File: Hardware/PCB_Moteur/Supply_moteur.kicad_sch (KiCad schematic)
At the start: 27 parts, among them J1 XT30PW-F, U1 L6981N33DR

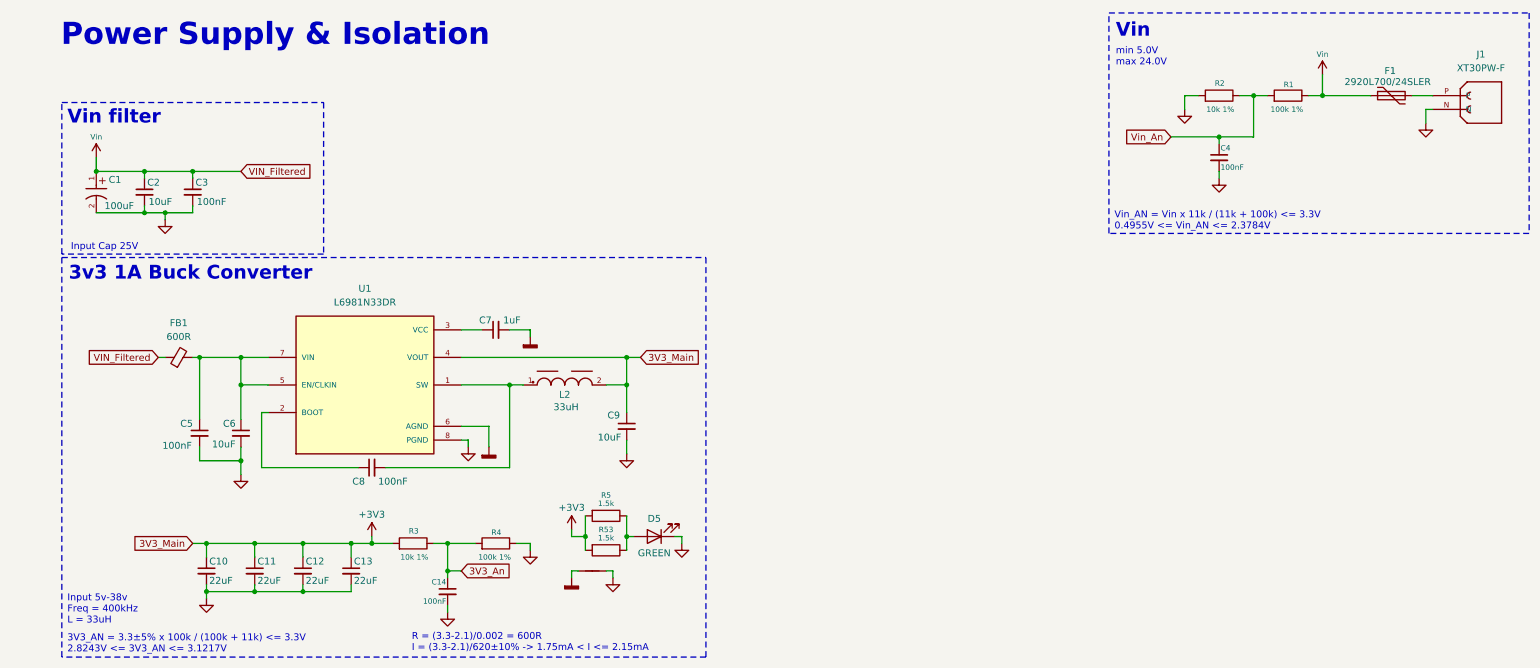
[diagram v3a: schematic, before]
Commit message: wip : reorder refdes and fix footprints
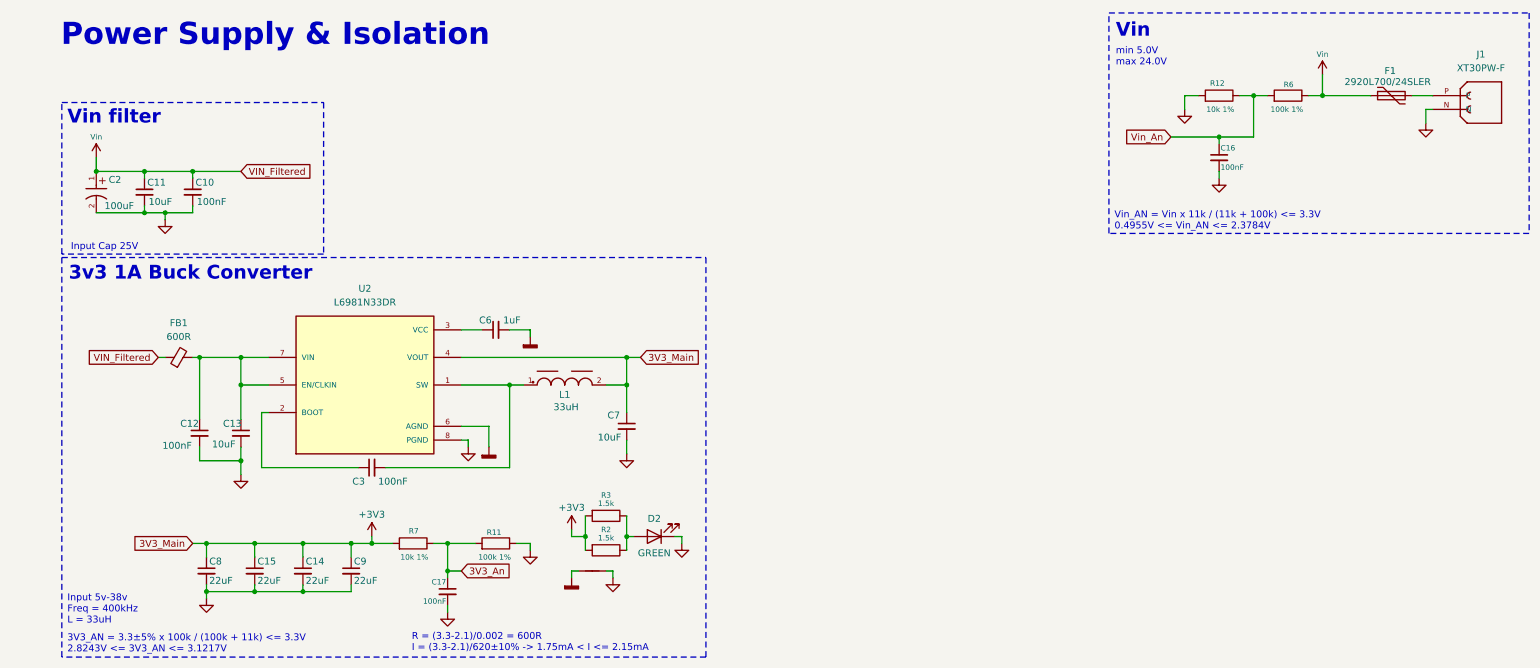
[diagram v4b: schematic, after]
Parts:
- renumbered C3 to C10, C2 to C11, C5 to C12, C6 to C13, C12 to C14, C11 to C15, C4 to C16, C14 to C17, C1 to C2, C8 to C3, C7 to C6, C9 to C7, C10 to C8, C13 to C9, D5 to D2, L2 to L1, NT4 to NT0, R4 to R11, R2 to R12, R53 to R2, R5 to R3, R1 to R6, R3 to R7, U1 to U2
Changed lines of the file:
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@@
 		(on_board yes)
 		(dnp no)
-		(property "Reference" "R4"
+		(property "Reference" "R11"
 			(at 94.996 108.458 90)
 			(effects
@@
 			(project "PCB_moteur"
 				(path "/b0d87684-7b1c-41d8-8358-755aa327573e/92d1df5d-a307-4eea-a65c-ade4cb0ad548"
-					(reference "R4")
+					(reference "R11")
 					(unit 1)
 				)
@@
 		(dnp no)
 		(fields_autoplaced yes)
-		(property "Reference" "NT4"
+		(property "Reference" "NT0"
 			(at 111.76 110.49 0)
 			(effects
@@
 			(project "PCB_moteur"
 				(path "/b0d87684-7b1c-41d8-8358-755aa327573e/92d1df5d-a307-4eea-a65c-ade4cb0ad548"
-					(reference "NT4")
+					(reference "NT0")
 					(unit 1)
 				)
@@
 		(on_board yes)
 		(dnp no)
-		(property "Reference" "C11"
+		(property "Reference" "C15"
 			(at 50.038 113.792 0)
 			(effects
@@
 			(project "PCB_moteur"
 				(path "/b0d87684-7b1c-41d8-8358-755aa327573e/92d1df5d-a307-4eea-a65c-ade4cb0ad548"
-					(reference "C11")
+					(reference "C15")
 					(unit 1)
 				)
@@
 		(on_board yes)
 		(dnp no)
-		(property "Reference" "R3"
+		(property "Reference" "R7"
 			(at 79.756 108.204 90)
 			(effects
@@
 			(project "PCB_moteur"
 				(path "/b0d87684-7b1c-41d8-8358-755aa327573e/92d1df5d-a307-4eea-a65c-ade4cb0ad548"
-					(reference "R3")
+					(reference "R7")
 					(unit 1)
 				)
@@
 		(on_board yes)
 		(dnp no)
-		(property "Reference" "R2"
+		(property "Reference" "R12"
 			(at 228.346 25.654 90)
 			(effects
@@
 			(project "PCB_moteur"
 				(path "/b0d87684-7b1c-41d8-8358-755aa327573e/92d1df5d-a307-4eea-a65c-ade4cb0ad548"
-					(reference "R2")
+					(reference "R12")
 					(unit 1)
 				)
@@
 		(on_board yes)
 		(dnp no)
-		(property "Reference" "D5"
+		(property "Reference" "D2"
 			(at 123.19 105.918 0)
 			(effects
@@
 			(project "PCB_moteur"
 				(path "/b0d87684-7b1c-41d8-8358-755aa327573e/92d1df5d-a307-4eea-a65c-ade4cb0ad548"
-					(reference "D5")
+					(reference "D2")
 					(unit 1)
 				)
@@
 		(on_board yes)
 		(dnp no)
-		(property "Reference" "C6"
+		(property "Reference" "C13"
 			(at 43.688 88.392 0)
 			(effects
@@
 			(project "PCB_moteur"
 				(path "/b0d87684-7b1c-41d8-8358-755aa327573e/92d1df5d-a307-4eea-a65c-ade4cb0ad548"
-					(reference "C6")
+					(reference "C13")
 					(unit 1)
 				)
@@
 		(on_board yes)
 		(dnp no)
-		(property "Reference" "C7"
+		(property "Reference" "C6"
 			(at 93.218 69.342 90)
 			(effects
@@
 			(project "PCB_moteur"
 				(path "/b0d87684-7b1c-41d8-8358-755aa327573e/92d1df5d-a307-4eea-a65c-ade4cb0ad548"
-					(reference "C7")
+					(reference "C6")
 					(unit 1)
 				)
@@
 		(on_board yes)
 		(dnp no)
-		(property "Reference" "L2"
+		(property "Reference" "L1"
 			(at 106.68 83.058 0)
 			(effects
@@
 			(project "PCB_moteur"
 				(path "/b0d87684-7b1c-41d8-8358-755aa327573e/92d1df5d-a307-4eea-a65c-ade4cb0ad548"
-					(reference "L2")
+					(reference "L1")
 					(unit 1)
 				)
@@
 		(on_board yes)
 		(dnp no)
-		(property "Reference" "C10"
+		(property "Reference" "C8"
 			(at 41.148 113.792 0)
 			(effects
@@
 			(project "PCB_moteur"
 				(path "/b0d87684-7b1c-41d8-8358-755aa327573e/92d1df5d-a307-4eea-a65c-ade4cb0ad548"
-					(reference "C10")
+					(reference "C8")
 					(unit 1)
 				)
@@
 		(on_board yes)
 		(dnp no)
-		(property "Reference" "C1"
+		(property "Reference" "C2"
 			(at 22.606 43.434 90)
 			(effects
@@
 			(project ""
 				(path "/b0d87684-7b1c-41d8-8358-755aa327573e/92d1df5d-a307-4eea-a65c-ade4cb0ad548"
-					(reference "C1")
+					(reference "C2")
 					(unit 1)
 				)
@@
 		(on_board yes)
 		(dnp no)
-		(property "Reference" "C14"
+		(property "Reference" "C17"
 			(at 84.836 117.602 0)
 			(effects
@@
 			(project "PCB_moteur"
 				(path "/b0d87684-7b1c-41d8-8358-755aa327573e/92d1df5d-a307-4eea-a65c-ade4cb0ad548"
-					(reference "C14")
+					(reference "C17")
 					(unit 1)
 				)
@@
 		(on_board yes)
 		(dnp no)
-		(property "Reference" "C4"
+		(property "Reference" "C16"
 			(at 227.584 37.592 0)
 			(effects
@@
 			(project "PCB_moteur"
 				(path "/b0d87684-7b1c-41d8-8358-755aa327573e/92d1df5d-a307-4eea-a65c-ade4cb0ad548"
-					(reference "C4")
+					(reference "C16")
 					(unit 1)
 				)
@@
 		(on_board yes)
 		(dnp no)
-		(property "Reference" "C9"
+		(property "Reference" "C7"
 			(at 114.554 86.868 0)
 			(effects
@@
 			(project "PCB_moteur"
 				(path "/b0d87684-7b1c-41d8-8358-755aa327573e/92d1df5d-a307-4eea-a65c-ade4cb0ad548"
-					(reference "C9")
+					(reference "C7")
 					(unit 1)
 				)
@@
 		(on_board yes)
 		(dnp no)
-		(property "Reference" "C2"
+		(property "Reference" "C11"
 			(at 29.718 43.942 0)
 			(effects
@@
 			(project "PCB_moteur"
 				(path "/b0d87684-7b1c-41d8-8358-755aa327573e/92d1df5d-a307-4eea-a65c-ade4cb0ad548"
-					(reference "C2")
+					(reference "C11")
 					(unit 1)
 				)
@@
 		(on_board yes)
 		(dnp no)
-		(property "Reference" "R53"
+		(property "Reference" "R2"
 			(at 114.3 107.95 90)
 			(effects
@@
 			(project "PCB_moteur"
 				(path "/b0d87684-7b1c-41d8-8358-755aa327573e/92d1df5d-a307-4eea-a65c-ade4cb0ad548"
-					(reference "R53")
+					(reference "R2")
 					(unit 1)
 				)
@@
 		(on_board yes)
 		(dnp no)
-		(property "Reference" "R5"
+		(property "Reference" "R3"
 			(at 114.3 101.6 90)
 			(effects
@@
 			(project "PCB_moteur"
 				(path "/b0d87684-7b1c-41d8-8358-755aa327573e/92d1df5d-a307-4eea-a65c-ade4cb0ad548"
-					(reference "R5")
+					(reference "R3")
 					(unit 1)
 				)
@@
 		(on_board yes)
 		(dnp no)
-		(property "Reference" "C8"
+		(property "Reference" "C3"
 			(at 69.85 99.06 90)
 			(effects
@@
 			(project "PCB_moteur"
 				(path "/b0d87684-7b1c-41d8-8358-755aa327573e/92d1df5d-a307-4eea-a65c-ade4cb0ad548"
-					(reference "C8")
+					(reference "C3")
 					(unit 1)
 				)
@@
 		(on_board yes)
 		(dnp no)
-		(property "Reference" "C5"
+		(property "Reference" "C12"
 			(at 35.814 88.392 0)
 			(effects
@@
 			(project "PCB_moteur"
 				(path "/b0d87684-7b1c-41d8-8358-755aa327573e/92d1df5d-a307-4eea-a65c-ade4cb0ad548"
-					(reference "C5")
+					(reference "C12")
 					(unit 1)
 				)
@@
 		(on_board yes)
 		(dnp no)
-		(property "Reference" "C3"
+		(property "Reference" "C10"
 			(at 38.608 43.942 0)
 			(effects
@@
 			(project "PCB_moteur"
 				(path "/b0d87684-7b1c-41d8-8358-755aa327573e/92d1df5d-a307-4eea-a65c-ade4cb0ad548"
-					(reference "C3")
+					(reference "C10")
 					(unit 1)
 				)
@@
 		(on_board yes)
 		(dnp no)
-		(property "Reference" "C12"
+		(property "Reference" "C14"
 			(at 58.928 113.792 0)
 			(effects
@@
 			(project "PCB_moteur"
 				(path "/b0d87684-7b1c-41d8-8358-755aa327573e/92d1df5d-a307-4eea-a65c-ade4cb0ad548"
-					(reference "C12")
+					(reference "C14")
 					(unit 1)
 				)
@@
 		(dnp no)
 		(fields_autoplaced yes)
-		(property "Reference" "U1"
+		(property "Reference" "U2"
 			(at 69.85 63.5 0)
 			(effects
@@
 			(project ""
 				(path "/b0d87684-7b1c-41d8-8358-755aa327573e/92d1df5d-a307-4eea-a65c-ade4cb0ad548"
-					(reference "U1")
+					(reference "U2")
 					(unit 1)
 				)
@@
 		(on_board yes)
 		(dnp no)
-		(property "Reference" "R1"
+		(property "Reference" "R6"
 			(at 241.046 25.908 90)
 			(effects
@@
 			(project "PCB_moteur"
 				(path "/b0d87684-7b1c-41d8-8358-755aa327573e/92d1df5d-a307-4eea-a65c-ade4cb0ad548"
-					(reference "R1")
+					(reference "R6")
 					(unit 1)
 				)
@@
 		(on_board yes)
 		(dnp no)
-		(property "Reference" "C13"
+		(property "Reference" "C9"
 			(at 67.818 113.792 0)
 			(effects
@@
 			(project "PCB_moteur"
 				(path "/b0d87684-7b1c-41d8-8358-755aa327573e/92d1df5d-a307-4eea-a65c-ade4cb0ad548"
-					(reference "C13")
+					(reference "C9")
 					(unit 1)
 				)
